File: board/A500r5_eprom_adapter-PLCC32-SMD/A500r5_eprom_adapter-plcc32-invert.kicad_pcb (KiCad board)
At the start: 2 copper layers, 40.6 x 54.6 mm, 11 parts, among them J2 A18 Selector, J3 A19 Selector, U1 27C400-A500, U2 27C080-L, U3 27C080-L

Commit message: Add rev.2 boards
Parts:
- added J4: A17 Selector, Connector_PinHeader_2.54mm:PinHeader_1x03_P2.54mm_Vertical, F.Cu at (130.8, 96.5)
- turned C1 to 270 degrees
- turned C2 to 270 degrees
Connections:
- U1 pad 1: (no net) -> /SOCK_P1
- U1 pad 31: /A17 -> /SOCK_P31
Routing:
- net /A0: track 61.1 -> 107.3 mm, vias 1 -> 0
- net /SOCK_P1: track 0.00 -> 37.5 mm, vias 0 -> 2
- net /~OE: track 98.5 -> 68.9 mm, vias 0 -> 1
- net /D3-L: track 64.8 -> 93.5 mm, vias 1 -> 0
- net /~CE: track 67.0 -> 95.4 mm, vias 1 -> 0
- net /A7: track 89.9 -> 62.4 mm, vias 1 -> 0
- net /A3: track 87.7 -> 63.4 mm, vias 1 -> 0
- net /A9: track 77.1 -> 59.4 mm, vias 0 -> 1
- net /D7-L: track 36.1 -> 52.8 mm, vias 2 -> 1
- net /A15: track 56.3 -> 43.8 mm, vias 0 -> 1
- net /SOCK_P31: track 0.00 -> 10.3 mm
- net /A16: track 55.2 -> 45.1 mm, vias 0 -> 1
- net /A6: track 74.2 -> 64.5 mm, vias 1 -> 0
- net /D6-L: track 33.2 -> 41.8 mm, vias 1 -> 2
- net /D4-L: track 43.2 -> 51.3 mm
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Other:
- board text added: "-> 1"
- board text added: "31 <-"
- board text added: "A17"
- board text added: "Rev. 2"
- board text removed: "rev.1"

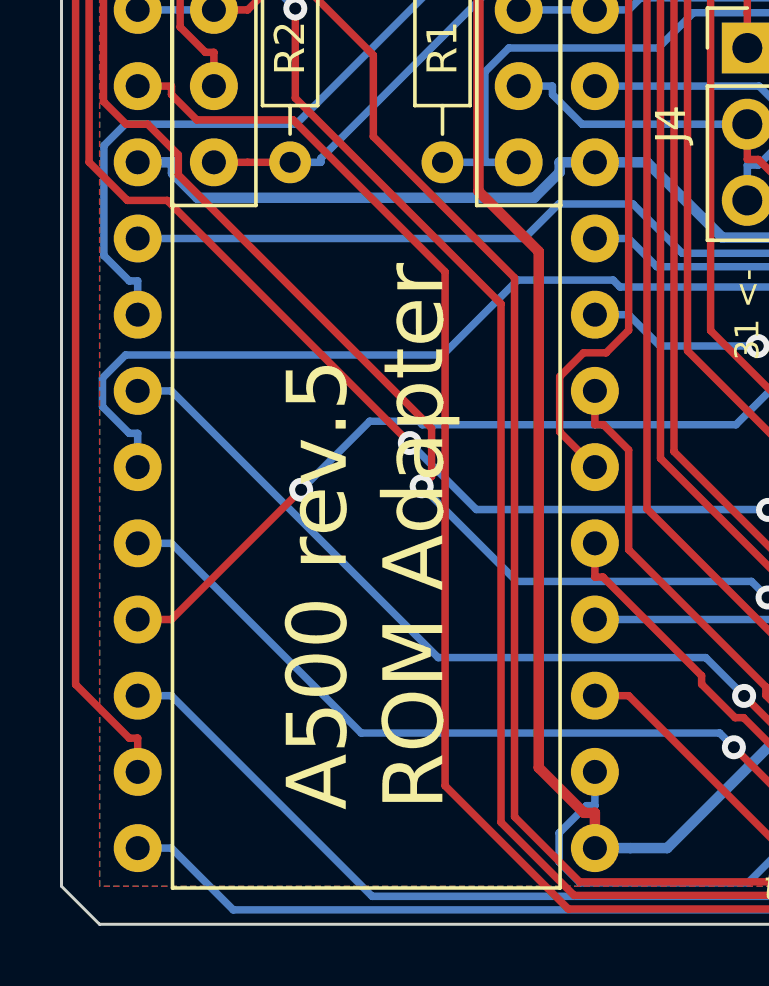
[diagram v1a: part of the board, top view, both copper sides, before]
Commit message: Cleanup silkscreen of PLCC32 version
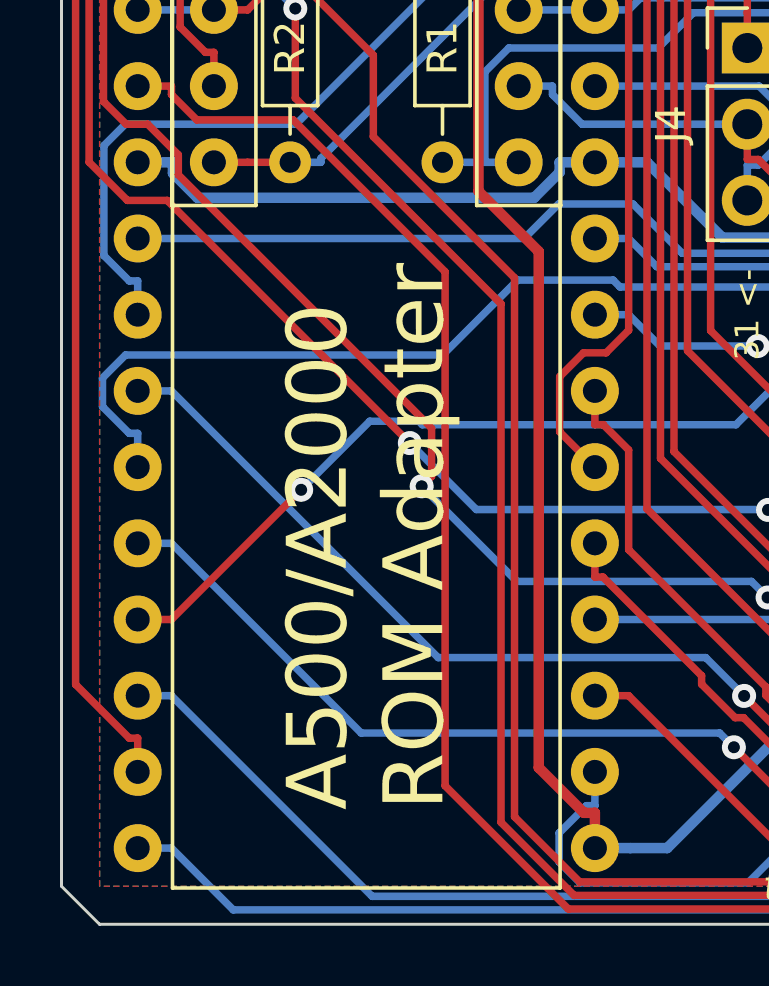
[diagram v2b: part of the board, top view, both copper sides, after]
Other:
- board text added: "A500/A2000 ROM Adapter"
- board text removed: "A500 rev.5 ROM Adapter"

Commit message: Updated PCB, getting ready for rev 3 of PLCC version, updated readme
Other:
- board text added: "Rev. 3"
- board text removed: "Rev. 2"

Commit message: Create an SMD rev 4
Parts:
- added RN3: 4.7K, Resistor_SMD:R_Array_Convex_4x0612, F.Cu at (123.3, 79.0)
- added RN4: 4.7K, Resistor_SMD:R_Array_Convex_4x0612, F.Cu at (123.3, 89.2)
- added RN5: 4.7K, Resistor_SMD:R_Array_Convex_4x0612, F.Cu at (117.0, 103.3)
- C1, C2: footprint Capacitor_SMD:C_1206_3216Metric -> Capacitor_SMD:C_0603_1608Metric_Pad1.08x0.95mm_HandSolder
- J2, J3: footprint Connector_PinHeader_2.54mm:PinHeader_1x02_P2.54mm_Vertical -> Jumper:SolderJumper-2_P1.3mm_Open_RoundedPad1.0x1.5mm
- J4: footprint Connector_PinHeader_2.54mm:PinHeader_1x03_P2.54mm_Vertical -> Jumper:SolderJumper-3_P1.3mm_Open_RoundedPad1.0x1.5mm
- R1, R2: value 4k7 -> 4.7K; footprint Resistor_THT:R_Axial_DIN0204_L3.6mm_D1.6mm_P7.62mm_Horizontal -> Resistor_SMD:R_0603_1608Metric_Pad0.98x0.95mm_HandSolder
- RN1, RN2: value 4k7 -> 4.7K; footprint Resistor_THT:R_Array_SIP11 -> Resistor_SMD:R_Array_Convex_4x0612
- U2, U3: moved to B.Cu
- moved J4 27.3 mm to (114.0, 74.9)
- moved J2 27.3 mm to (115.3, 110.1)
- moved J3 23.9 mm to (117.9, 110.1)
- moved C1 23.6 mm to (117.8, 102.9), turned to 0 degrees
- moved C2 22.2 mm to (117.8, 75.7), turned to 0 degrees
- moved U2 20.4 mm to (118.1, 85.6), turned to 180 degrees
- moved U3 20.3 mm to (118.1, 113.3), turned to 180 degrees
- moved RN2 19.1 mm to (113.2, 91.2), turned to 180 degrees
- moved R1 14.9 mm to (115.3, 106.6), turned to 90 degrees
- moved R2 14.1 mm to (117.9, 106.6), turned to 90 degrees
- moved RN1 6.35 mm to (113.2, 81.3), turned to 180 degrees
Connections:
- net /~CE renamed /~{CE}
- net /~OE renamed /~{OE}
- R1 pad 1: VCC -> /A18
- R1 pad 2: /A18 -> VCC
- R2 pad 1: VCC -> /A19
- R2 pad 2: /A19 -> VCC
- RN1 pad 2: /A7 -> VCC
- RN1 pad 3: /A6 -> VCC
- RN1 pad 4: /A5 -> VCC
- RN1 pad 5: /A4 -> /A7
- RN1 pad 6: /A3 -> /A6
- RN1 pad 7: /A2 -> /A5
- RN1 pad 8: /A1 -> /A4
- RN2 pad 2: /A9 -> VCC
- RN2 pad 3: /A10 -> VCC
- RN2 pad 4: /A11 -> VCC
- RN2 pad 5: /A12 -> /A3
- RN2 pad 6: /A13 -> /A2
- RN2 pad 7: /A14 -> /A1
- RN2 pad 8: /A15 -> /A0
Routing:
- net /D3-L: track 93.5 -> 33.4 mm, vias 0 -> 1
- net /~{CE}: track 95.4 -> 39.3 mm, vias 0 -> 3
- net /A4: track 106.3 -> 52.3 mm
- net /A0: track 107.3 -> 53.7 mm, vias 0 -> 3
- net /SOCK_P1: track 37.5 -> 2.26 mm, vias 2 -> 0
- net /~{OE}: track 68.9 -> 34.7 mm, vias 1 -> 2
- net /D7-L: track 52.8 -> 24.8 mm
- net /A5: track 74.5 -> 47.1 mm
- net /A19: track 68.7 -> 41.5 mm, vias 0 -> 2
- net GND: track 70.2 -> 96.5 mm
- net /A8: track 88.8 -> 64.4 mm, vias 2 -> 1
- net /D3-H: track 30.6 -> 9.07 mm, vias 1 -> 0
- net /D1-L: track 43.3 -> 23.4 mm
- net /A2: track 67.7 -> 48.8 mm, vias 2 -> 1
- net /D2-H: track 29.8 -> 11.4 mm
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- added copper zone on In1.Cu, net GND
- added copper zone on In2.Cu, net GND
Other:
- board size 40.6 x 54.6 mm -> 17.4 x 51.4 mm
- copper layers 2 -> 4
- net class Default removed
- net class POWER removed
- board text added: "1-2: A17 Pin 1 2-3: A17 Pin 31"
- board text added: "A500/A200 EPROM Adapter"
- board text added: "Populate R1 & R2 only if RNs are not populated!"
- board text added: "Rev. 4"
- board text removed: "-> 1"
- board text removed: "27C040/27C080"
- board text removed: "31 <-"
- board text removed: "A17"
- board text removed: "A500/A2000 ROM Adapter"
- board text removed: "HIGH"
- board text removed: "LOW"
- board text removed: "Rev. 3"
- board text removed: "tabaglio@posteo.net"

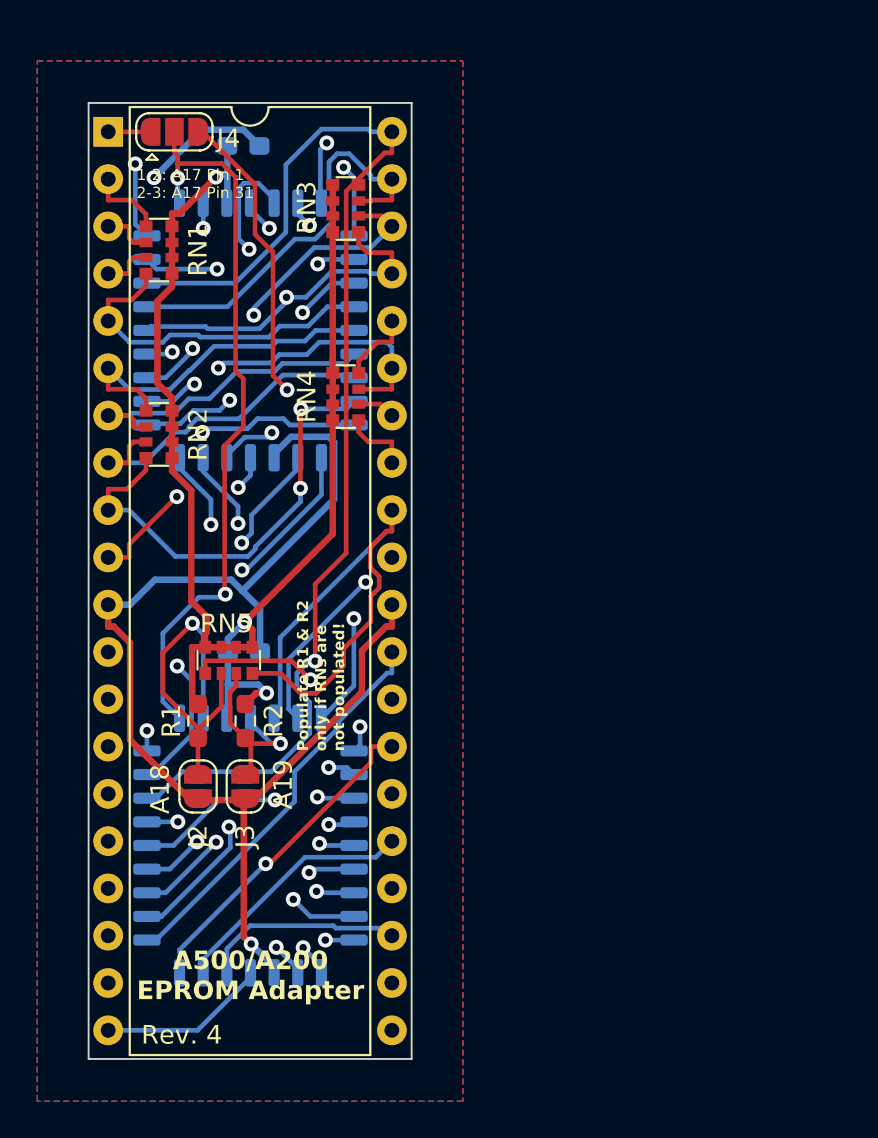
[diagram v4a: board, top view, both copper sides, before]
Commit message: Update the PLCC adapter
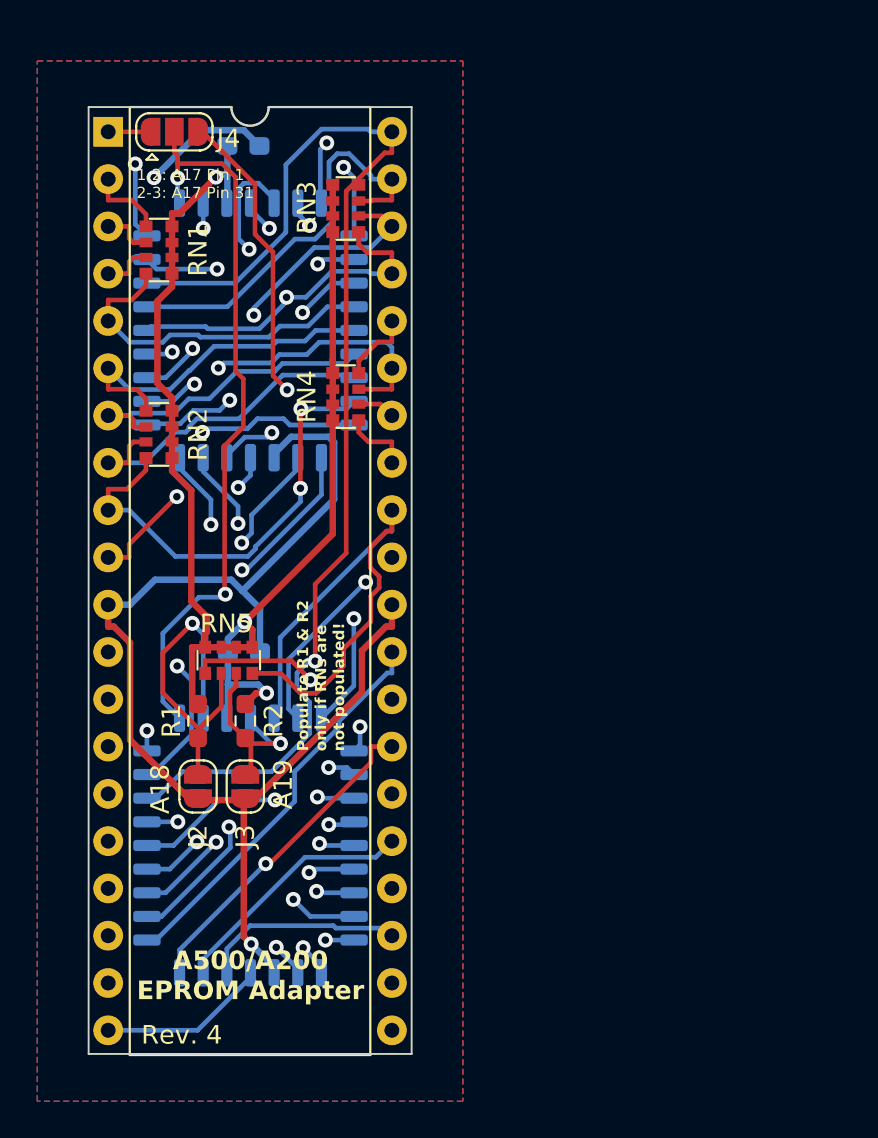
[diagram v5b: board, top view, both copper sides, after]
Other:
- board size 17.4 x 51.4 mm -> 17.4 x 50.9 mm
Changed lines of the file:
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@@
 	)
 	(gr_line
-		(start 126.79 73.38)
-		(end 126.79 124.73)
+		(start 126.79 73.6)
+		(end 126.79 124.46)
 		(stroke
 			(width 0.1)
@@
 	)
 	(gr_line
-		(start 126.79 124.73)
-		(end 109.44 124.73)
+		(start 126.79 124.46)
+		(end 109.44 124.46)
+		(stroke
+			(width 0.1)
+			(type default)
+		)
+		(layer "Edge.Cuts")
+	)
+	(gr_arc
+		(start 119.121 73.6)
+		(mid 118.11 74.611)
+		(end 117.099 73.6)
 		(stroke
 			(width 0.1)
@@
 	)
 	(gr_line
-		(start 109.44 73.38)
-		(end 126.79 73.38)
+		(start 109.44 73.6)
+		(end 117.099 73.6)
 		(stroke
 			(width 0.1)
@@
 	)
 	(gr_line
-		(start 109.44 124.73)
-		(end 109.44 73.38)
+		(start 119.121 73.6)
+		(end 126.79 73.6)
+		(stroke
+			(width 0.1)
+			(type default)
+		)
+		(layer "Edge.Cuts")
+	)
+	(gr_line
+		(start 109.44 124.46)
+		(end 109.44 73.6)
 		(stroke
 			(width 0.1)
@@
 	)
 	(segment
-		(start 117.7444 74.8184)
-		(end 118.618 75.692)
+		(start 112.9533 77.3934)
+		(end 115.23935 75.10735)
 		(width 0.35)
 		(layer "B.Cu")
@@
 	)
 	(segment
-		(start 115.5283 74.8184)
-		(end 117.7444 74.8184)
-		(width 0.35)
-		(layer "B.Cu")
-		(net 1)
-	)
-	(segment
 		(start 118.648 102.87)
 		(end 118.648 100.5324)
@@
 	)
 	(segment
+		(start 118.618 75.692)
+		(end 117.768 74.842)
+		(width 0.35)
+		(layer "B.Cu")
+		(net 1)
+	)
+	(segment
 		(start 122.6279 94.6645)
 		(end 122.6279 91.6023)
@@
 	)
 	(segment
+		(start 115.5047 74.842)
+		(end 115.23935 75.10735)
+		(width 0.35)
+		(layer "B.Cu")
+		(net 1)
+	)
+	(segment
 		(start 110.49 100.33)
 		(end 111.6667 100.33)
@@
 	)
 	(segment
-		(start 112.9533 77.3934)
-		(end 115.5283 74.8184)
-		(width 0.35)
-		(layer "B.Cu")
-		(net 1)
-	)
-	(segment
 		(start 113.0081 98.9886)
 		(end 111.6667 100.33)
@@
 		(width 0.35)
 		(layer "B.Cu")
+		(net 1)
+	)
+	(segment
+		(start 117.768 74.842)
+		(end 115.5047 74.842)
+		(width 0.35)
+		(layer "B.Cu")

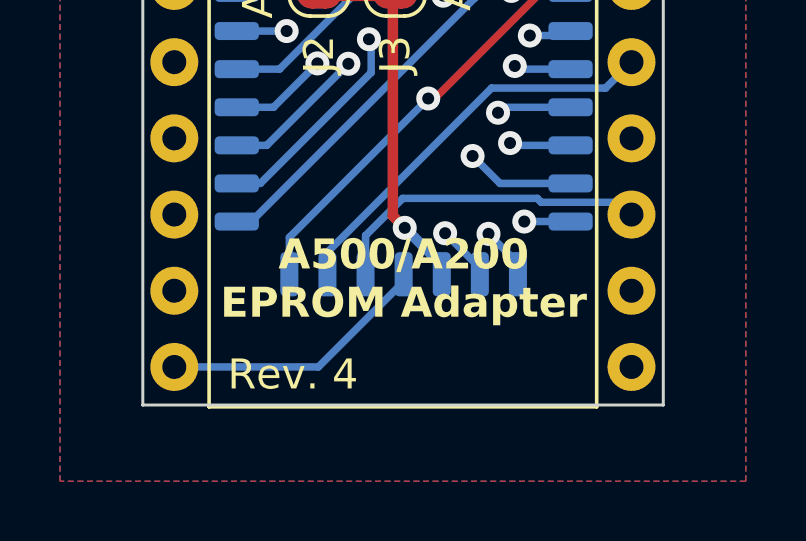
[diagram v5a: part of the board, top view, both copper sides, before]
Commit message: Fix "A2000" silkscreen in PLCC and TSOP adapter variants
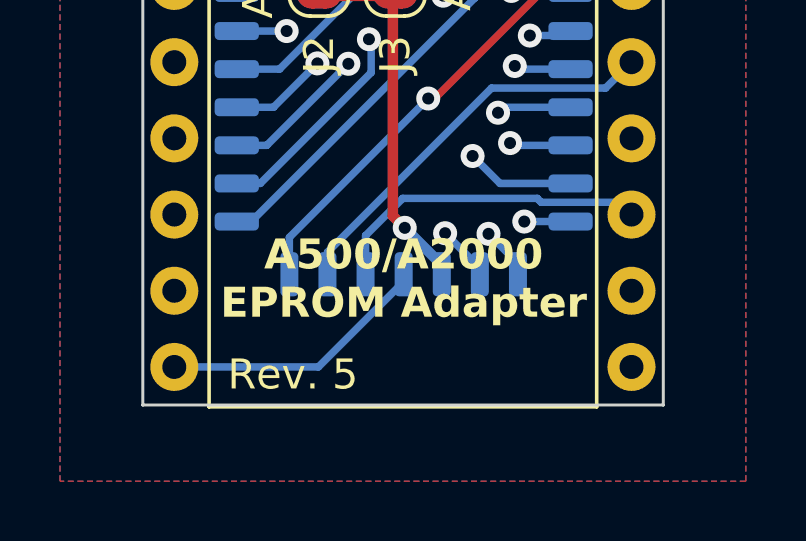
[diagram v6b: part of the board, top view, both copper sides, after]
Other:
- board text added: "A500/A2000 EPROM Adapter"
- board text added: "Rev. 5"
- board text removed: "A500/A200 EPROM Adapter"
- board text removed: "Rev. 4"
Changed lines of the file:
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@@
 			(drillshape 0)
 			(scaleselection 1)
-			(outputdirectory "gerbers/rev4/")
+			(outputdirectory "gerbers/rev5/")
 		)
 	)
@@
 		)
 	)
-	(gr_text "A500/A200\nEPROM Adapter"
+	(gr_text "A500/A2000\nEPROM Adapter"
 		(at 118.1355 120.2485 0)
 		(layer "F.SilkS")
@@
 		)
 	)
-	(gr_text "Rev. 4"
+	(gr_text "Rev. 5"
 		(at 112.268 123.444 0)
 		(layer "F.SilkS")
